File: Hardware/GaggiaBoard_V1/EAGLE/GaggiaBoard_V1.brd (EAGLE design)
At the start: 87 x 122 mm, 112 parts, among them IC1 LD117ADT33TR, J10 PIN262409-1, J11 PIN262409-1, J12 PIN262409-1, J13 PIN262409-1, J14 PIN262409-1, J15 PIN262409-1, J16 PIN262409-1, J17 PIN262409-1, J18 PIN262409-1, J19 PIN262409-1, J2 QWIIC_RIGHT_ANGLE, J20 PIN262409-1, J21 PIN262409-1, J22 PIN262409-1, J23 PIN262409-1, J24 5033981892, J3 QWIIC_RIGHT_ANGLE, J4 1X2-3.5MM, J5 1X2-3.5MM, K1 RELAY-SPDT-JZC-11F, K2 RELAY-SPDT-JZC-11F, K3 RELAY-SPDT-JZC-11F, Q1 600mA/40V, Q2 600mA/40V, Q3 600mA/40V, Q4 600mA/40V, Q5 600mA/40V, Q6 600mA/40V, Q8 600mA/40V, Q9 600mA/40V, U1 BLACKPILL, U2 MAX31855K, U3 MAX31855K, U5 TXS0102, U6 TXU0102

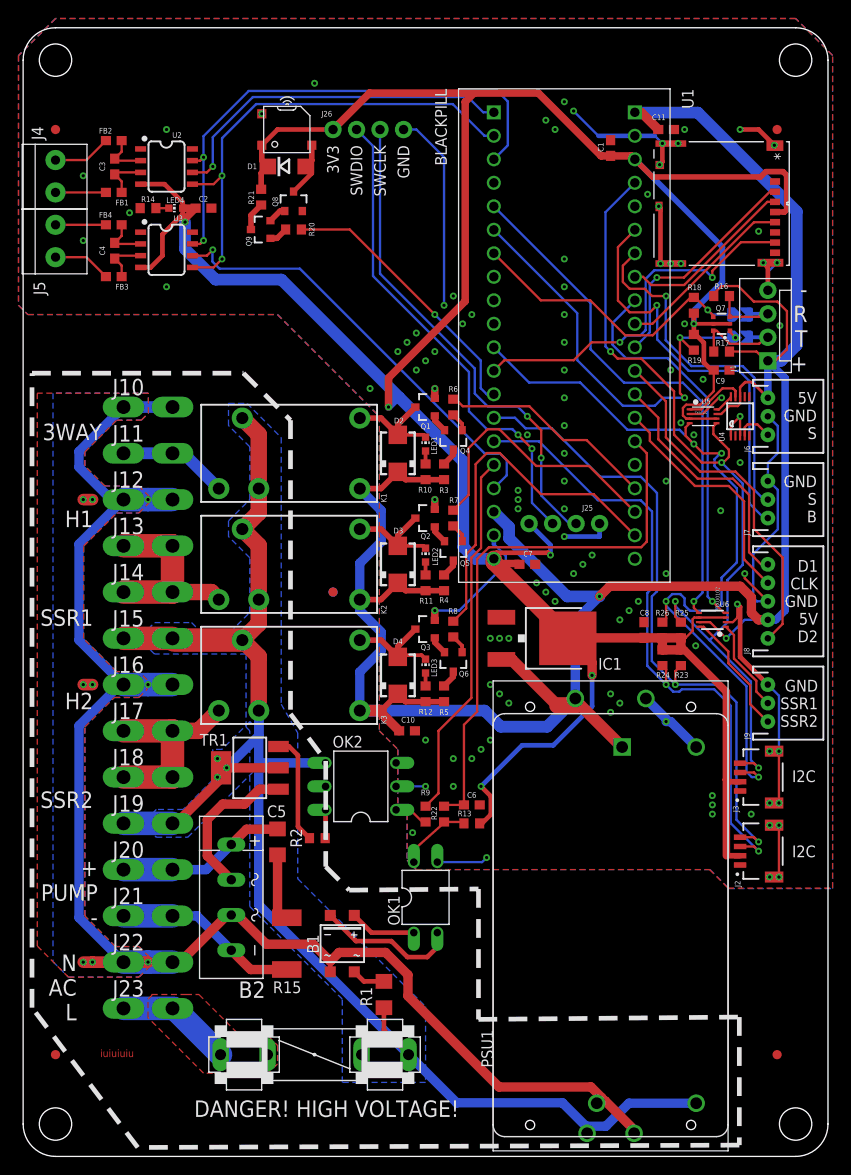
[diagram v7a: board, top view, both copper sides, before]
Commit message: UARTs reassigned, LEDs fixed
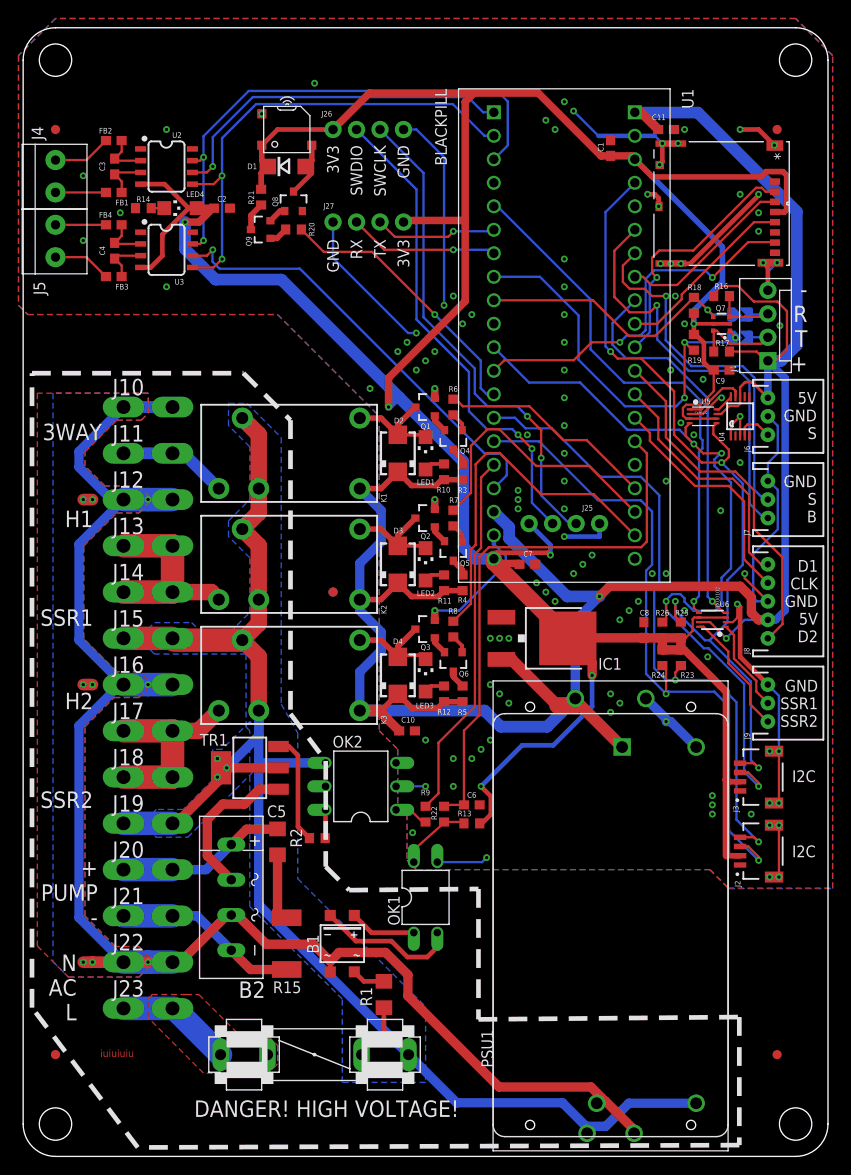
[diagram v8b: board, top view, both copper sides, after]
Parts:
- added J27: (no value), SparkFun-Connectors:1X04_NO_SILK
- LED1, LED2, LED3, LED4: device led:CHIP-LED0603 -> adafruit:CHIPLED_1206
- R6: value 10k -> 10K
- moved C2 2.00 mm to (18.0, 91.5)
- moved R10 2.00 mm to (42.0, 63.0)
- moved R11 2.00 mm to (42.0, 51.0)
- moved R12 2.00 mm to (42.0, 39.0)
- moved R3 2.00 mm to (44.0, 63.0)
- moved R4 2.00 mm to (44.0, 51.0)
- moved R5 2.00 mm to (44.0, 39.0)
- moved LED1 1.00 mm to (40.0, 65.0)
- moved LED2 1.00 mm to (40.0, 53.0)
- moved LED3 1.00 mm to (40.0, 41.0)
- moved LED4 0.50 mm to (13.5, 91.5)
- moved R14 0.50 mm to (9.50, 91.5)
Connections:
- net UART1_5V_RX renamed UART6_5V_RX
- net UART1_5V_TX renamed UART6_5V_TX
- new net UART6_RX: Q7.4, R18.1, SJ2.1, U1.P1$9
- new net UART6_TX: Q7.1, R19.1, SJ1.1, U1.P1$8
- net 3V3: now also J27.1
- net GND: now also J27.4
- net UART1_RX: now also J27.3; no longer Q7.4, R18.1, SJ2.1
- net UART1_TX: now also J27.2; no longer Q7.1, R19.1, SJ1.1
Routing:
- net UART6_TX: track 0.00 -> 44.2 mm, vias 0 -> 3
- net UART1_TX: track 48.1 -> 13.3 mm, vias 3 -> 1
- net UART6_RX: track 0.00 -> 30.7 mm, vias 0 -> 1
- net GND: track 159.3 -> 183.1 mm, vias 109 -> 115
- net UART1_RX: track 32.7 -> 16.2 mm
- net 3V3: track 338.3 -> 349.5 mm
- net 5V: track 272.5 -> 280.2 mm
- net I2C1_SDA: track 69.5 -> 72.7 mm
- net SPI1_NSS: track 25.2 -> 27.5 mm
- net N$29: track 1.40 -> 2.25 mm
- net N$28: track 1.40 -> 2.25 mm
- net N$24: track 1.40 -> 2.25 mm
- net I2C2_SDA: track 86.6 -> 87.4 mm
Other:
- board text added: "GND RX TX 3V3"
